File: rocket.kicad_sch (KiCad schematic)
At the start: 0 parts

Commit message: Place components
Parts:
- added A1: RaspberryPi_Pico, Module:RaspberryPi_Pico_Common_Unspecified, symbol MCU_Module:RaspberryPi_Pico
- added H1: MountingHole_Pad, MountingHole:MountingHole_2.2mm_M2_ISO7380_Pad_TopBottom, symbol Mechanical:MountingHole_Pad
- added H2, H3, H4: MountingHole_Pad, symbol Mechanical:MountingHole_Pad
- added J2: Micro_SD_Card, Connector_Card:microSD_HC_Wuerth_693072010801, symbol Connector:Micro_SD_Card
- added U1, U4: ICM-20948, Sensor_Motion:InvenSense_QFN-24_3x3mm_P0.4mm, symbol Sensor_Motion:ICM-20948
- added U2: RFM69HW, RF_Module:HOPERF_RFM69HW, symbol RF_Module:RFM69HW
- added U3: BMP390, 10LGA_2X2X0p75_BOS, symbol BMP390:BMP390
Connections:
- new net: U2.11 (GND), U2.9 (GND)
- new net: A1.13 (GND), A1.18 (GND), A1.23 (GND), A1.28 (GND), A1.3 (GND), A1.38 (GND), A1.8 (GND)
- new net: U4.18 (GND), U4.20 (GND)
- new net: U1.18 (GND), U1.20 (GND)
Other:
- title: (none) -> Rocketry Avionics Task

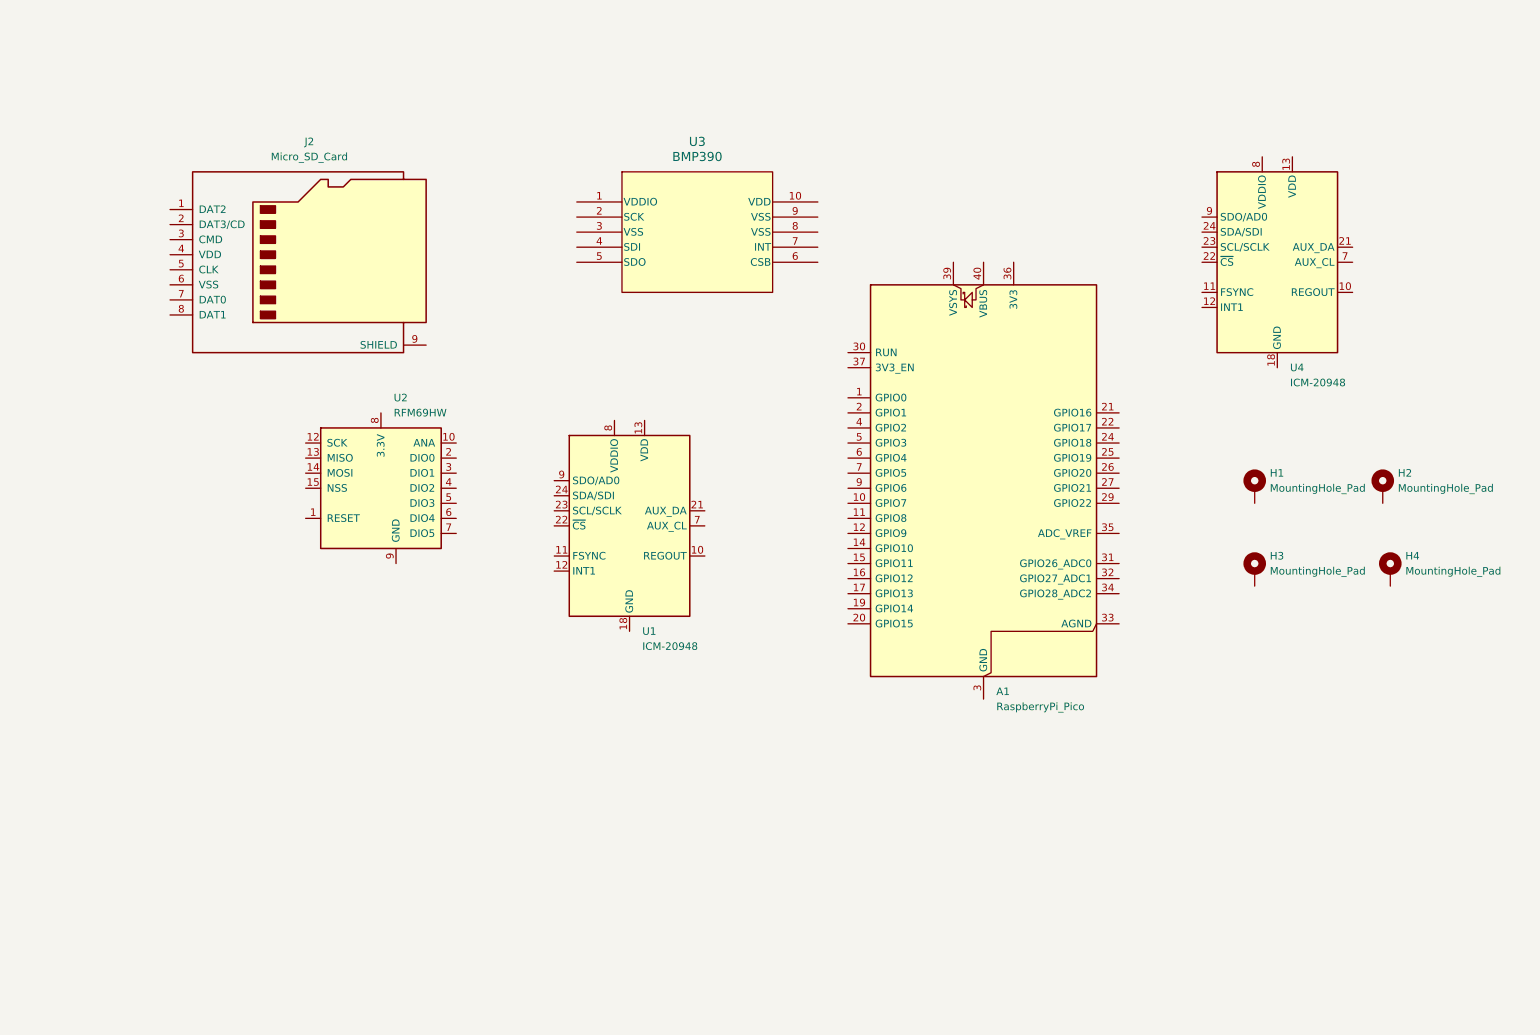
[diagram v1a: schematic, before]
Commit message: Logic level translators
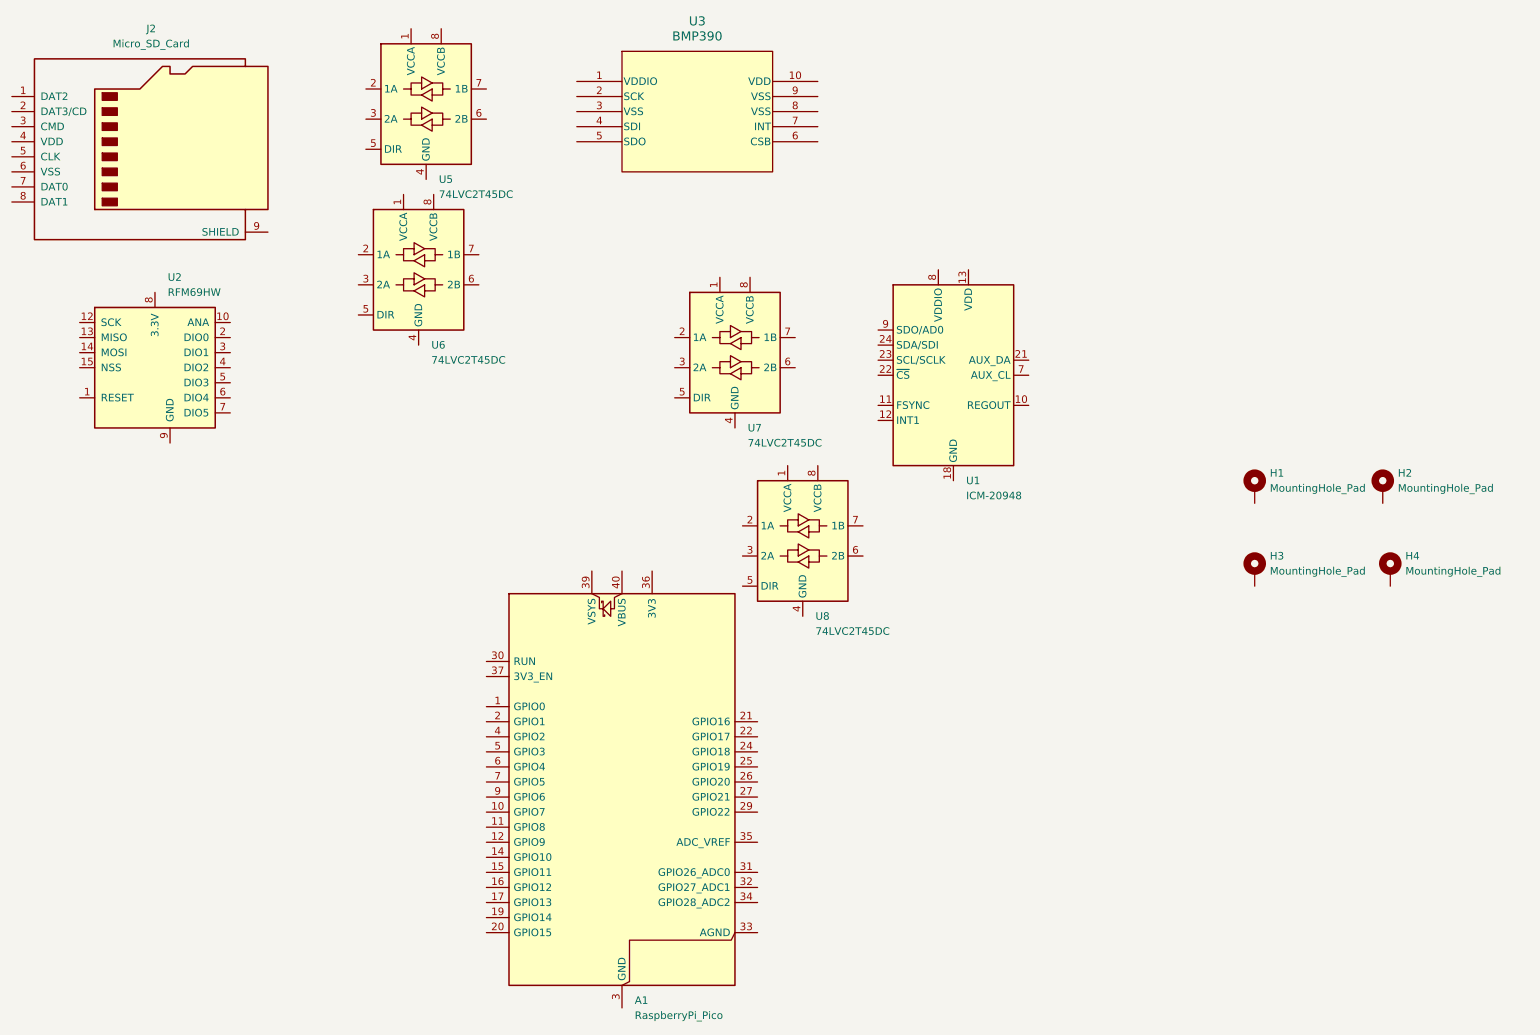
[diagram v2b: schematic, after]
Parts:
- removed U4: ICM-20948, Sensor_Motion:InvenSense_QFN-24_3x3mm_P0.4mm, symbol Sensor_Motion:ICM-20948
- added U5, U6, U7, U8: 74LVC2T45DC, Package_SO:VSSOP-8_2.3x2mm_P0.5mm, symbol Logic_LevelTranslator:74LVC2T45DC
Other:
- moved on the sheet: A1, J2, U1, U2, U3

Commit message: Wiring
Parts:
- removed J2: Micro_SD_Card, Connector_Card:microSD_HC_Wuerth_693072010801, symbol Connector:Micro_SD_Card
- removed U1: ICM-20948, Sensor_Motion:InvenSense_QFN-24_3x3mm_P0.4mm, symbol Sensor_Motion:ICM-20948
- removed U2: RFM69HW, RF_Module:HOPERF_RFM69HW, symbol RF_Module:RFM69HW
- removed U3: BMP390, 10LGA_2X2X0p75_BOS, symbol BMP390:BMP390
- removed U5, U6, U7, U8: 74LVC2T45DC, Package_SO:VSSOP-8_2.3x2mm_P0.5mm, symbol Logic_LevelTranslator:74LVC2T45DC
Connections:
- net Sensors/CS1: now reaches A1.12 (GPIO9)
- net Data Logging/VSS: now reaches A1.13 (GND), A1.18 (GND), A1.23 (GND), A1.28 (GND), A1.3 (GND), A1.38 (GND), A1.8 (GND)
- net Sensors/SCLK: now reaches A1.14 (GPIO10)
- net Sensors/MOSI: now reaches A1.15 (GPIO11)
- net Sensors/MISO: now reaches A1.16 (GPIO12)
- net Sensors/CS2: now reaches A1.17 (GPIO13)
- net Data Logging/CS1: now reaches A1.2 (GPIO1)
- net Data Logging/VDD: now reaches A1.36 (3V3)
- net Data Logging/SCLK: now reaches A1.4 (GPIO2)
- net Data Logging/MOSI: now reaches A1.5 (GPIO3)
- net Data Logging/MISO: now reaches A1.6 (GPIO4)
- net Data Logging/CS2: now reaches A1.7 (GPIO5)
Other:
- added sheet Data Logging (logging.kicad_sch)
- added sheet Sensors (sensors.kicad_sch)
- moved on the sheet: A1

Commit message: Power circuitry
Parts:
- removed H1: MountingHole_Pad, MountingHole:MountingHole_2.2mm_M2_ISO7380_Pad_TopBottom, symbol Mechanical:MountingHole_Pad
- removed H2: MountingHole_Pad, symbol Mechanical:MountingHole_Pad
- added H5, H6: MountingHole_Pad, MountingHole:MountingHole_2.5mm_Pad, symbol Mechanical:MountingHole_Pad
- added U1, U6: CPC1020N, Package_SO:SOP-4_3.8x4.1mm_P2.54mm, symbol Relay_SolidState:CPC1020N
- H3: renamed from H4; footprint (none) -> MountingHole:MountingHole_2.5mm_Pad
- H4: renamed from H3; footprint (none) -> MountingHole:MountingHole_2.5mm_Pad
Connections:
- net at H4.1: now also U1.4
- net at A1.21 (GPIO16): now also U1.1
- net at A1.22 (GPIO17): now also U6.1
- net Power circuitry/PGND: now reaches A1.33 (AGND)
- net Power circuitry/PGND: now also U1.2, U6.2
- net Power circuitry/7.4V: now reaches H3.1
- net Power circuitry/7.4V: now also H5.1
- new net: H6.1, U6.4
- new net Power circuitry/BGND: U1.3, U6.3
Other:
- added sheet Power circuitry (power.kicad_sch)
- moved on the sheet: H3, H4

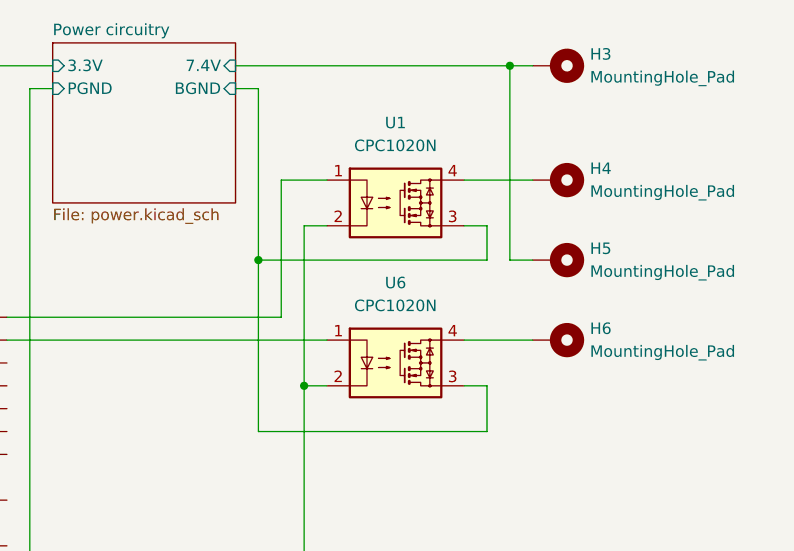
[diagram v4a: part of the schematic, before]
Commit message: Update references and switch to higher power MOSFETS
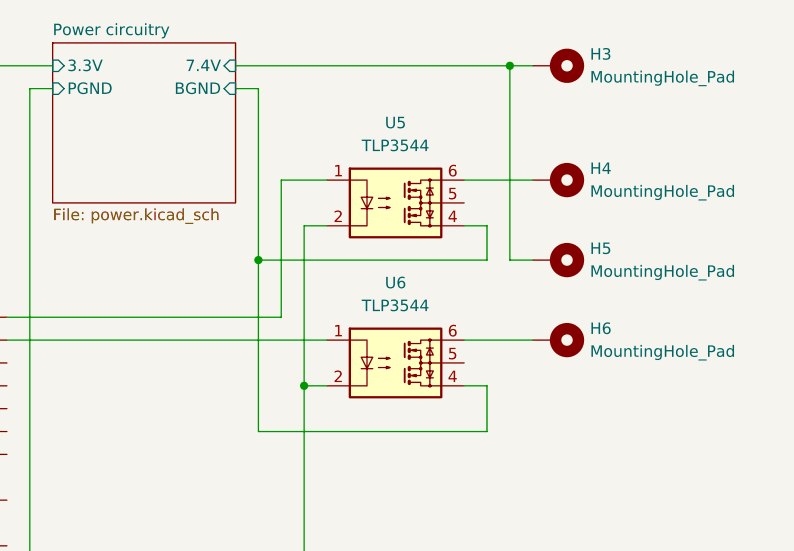
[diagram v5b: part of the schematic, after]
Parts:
- removed U1, U6: CPC1020N, Package_SO:SOP-4_3.8x4.1mm_P2.54mm, symbol Relay_SolidState:CPC1020N
- added U5, U6: TLP3544, Package_DIP:DIP-6_W7.62mm, symbol Relay_SolidState:TLP3544
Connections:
- net Power circuitry/BGND: now also U5.4, U6.4
- net Power circuitry/PGND: now also U5.2, U6.2
- net at H6.1: now also U6.6
- net at H4.1: now also U5.6
- net at A1.22 (GPIO17): now also U6.1
- net at A1.21 (GPIO16): now also U5.1
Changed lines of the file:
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@@
+	)
+	(symbol
+		(lib_id "Relay_SolidState:TLP3544")
+		(at 168.91 72.39 0)
+		(unit 1)
+		(exclude_from_sim no)
+		(in_bom yes)
+		(on_board yes)
+		(dnp no)
+		(fields_autoplaced yes)
+		(property "Reference" "U5"
+			(at 168.91 63.5 0)
+			(effects
+				(font
+					(size 1.27 1.27)
+				)
+			)
+		)
+		(property "Value" "TLP3544"
+			(at 168.91 66.04 0)
+			(effects
+				(font
+					(size 1.27 1.27)
+				)
+			)
+		)
+		(property "Footprint" "Package_DIP:DIP-6_W7.62mm"
+			(at 168.91 80.01 0)
+			(effects
+				(font
+					(size 1.27 1.27)
+				)
+				(hide yes)
+			)
+		)
+		(property "Datasheet" "https://toshiba.semicon-storage.com/info/docget.jsp?did=12661&prodName=TLP3544"
+			(at 168.91 72.39 0)
+			(effects
+				(font
+					(size 1.27 1.27)
+				)
+				(hide yes)
+			)
+		)
+		(property "Description" "Photo MOSFET optically coupled, ON 3.5A, 60mohm, OFF state 40V, Isolation 2500 VRMS, DIP-6"
+			(at 168.91 72.39 0)
+			(effects
+				(font
+					(size 1.27 1.27)
+				)
+				(hide yes)
+			)
+		)
+		(pin "4"
+		)
+		(pin "1"
+		)
+		(pin "5"
+		)
+		(pin "2"
+		)
+		(pin "6"
+		)
+		(pin "3"
+		)
+		(instances
+			(project ""
+				(path "/d94d1fd0-ec09-478b-a1a4-3306111fc872"
+					(reference "U5")
+					(unit 1)
+				)
+			)
+		)
 	)
 	(symbol
@@
 	)
 	(symbol
-		(lib_id "Relay_SolidState:CPC1020N")
+		(lib_id "Relay_SolidState:TLP3544")
 		(at 168.91 90.17 0)
 		(unit 1)
@@
 			)
 		)
-		(property "Value" "CPC1020N"
+		(property "Value" "TLP3544"
 			(at 168.91 83.82 0)
 			(effects
@@
 			)
 		)
-		(property "Footprint" "Package_SO:SOP-4_3.8x4.1mm_P2.54mm"
-			(at 168.91 95.504 0)
-			(effects
-				(font
-					(size 1.27 1.27)
-					(italic yes)
-				)
-				(hide yes)
-			)
-		)
-		(property "Datasheet" "https://www.littelfuse.com/assetdocs/littelfuse-integrated-circuits-cpc1020n-datasheet?assetguid=ccf92761-d571-4531-b987-0d7a91fc62dc"
-			(at 168.91 99.568 0)
-			(effects
-				(font
-					(size 1.27 1.27)
-				)
-				(hide yes)
-			)
-		)
-		(property "Description" "Form A, Solid State Relay (Photo MOSFET) 30V, 1.2A, 0.25Ohm, AC/DC, SO-4"
-			(at 168.91 97.536 0)
+		(property "Footprint" "Package_DIP:DIP-6_W7.62mm"
+			(at 168.91 97.79 0)
+			(effects
+				(font
+					(size 1.27 1.27)
+				)
+				(hide yes)
+			)
+		)
+		(property "Datasheet" "https://toshiba.semicon-storage.com/info/docget.jsp?did=12661&prodName=TLP3544"
+			(at 168.91 90.17 0)
+			(effects
+				(font
+					(size 1.27 1.27)
+				)
+				(hide yes)
+			)
+		)
+		(property "Description" "Photo MOSFET optically coupled, ON 3.5A, 60mohm, OFF state 40V, Isolation 2500 VRMS, DIP-6"
+			(at 168.91 90.17 0)
 			(effects
 				(font
@@
 		(pin "1"
 		)
+		(pin "5"
+		)
 		(pin "2"
+		)
+		(pin "6"
 		)
 		(pin "3"
@@
 					(unit 1)
 				)
-			)
-		)
-	)
-	(symbol
-		(lib_id "Relay_SolidState:CPC1020N")
-		(at 168.91 72.39 0)
-		(unit 1)
-		(exclude_from_sim no)
-		(in_bom yes)
-		(on_board yes)
-		(dnp no)
-		(fields_autoplaced yes)
-		(property "Reference" "U1"
-			(at 168.91 63.5 0)
-			(effects
-				(font
-					(size 1.27 1.27)
-				)
-			)
-		)
-		(property "Value" "CPC1020N"
-			(at 168.91 66.04 0)
-			(effects
-				(font
-					(size 1.27 1.27)
-				)
-			)
-		)
-		(property "Footprint" "Package_SO:SOP-4_3.8x4.1mm_P2.54mm"
-			(at 168.91 77.724 0)
-			(effects
-				(font
-					(size 1.27 1.27)
-					(italic yes)
-				)
-				(hide yes)
-			)
-		)
-		(property "Datasheet" "https://www.littelfuse.com/assetdocs/littelfuse-integrated-circuits-cpc1020n-datasheet?assetguid=ccf92761-d571-4531-b987-0d7a91fc62dc"
-			(at 168.91 81.788 0)
-			(effects
-				(font
-					(size 1.27 1.27)
-				)
-				(hide yes)
-			)
-		)
-		(property "Description" "Form A, Solid State Relay (Photo MOSFET) 30V, 1.2A, 0.25Ohm, AC/DC, SO-4"
-			(at 168.91 79.756 0)
-			(effects
-				(font
-					(size 1.27 1.27)
-				)
-				(hide yes)
-			)
-		)
-		(pin "4"
-		)
-		(pin "1"
-		)
-		(pin "2"
-		)
-		(pin "3"
-		)
-		(instances
-			(project ""
-				(path "/d94d1fd0-ec09-478b-a1a4-3306111fc872"
-					(reference "U1")
-					(unit 1)
-				)

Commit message: Begin PCB work
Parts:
- added R1, R2: 200Ω, Resistor_SMD:R_0201_0603Metric, symbol Device:R
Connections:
- net at U5.1: now also R1.2; no longer A1.21 (GPIO16)
- net at U6.1: now also R2.2; no longer A1.22 (GPIO17)
- new net: A1.21 (GPIO16), R1.1
- new net: A1.22 (GPIO17), R2.1
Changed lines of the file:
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@@
-	(wire
-		(pts
-			(xy 125.73 87.63) (xy 161.29 87.63)
-		)
-		(stroke
-			(width 0)
-			(type default)
-		)
-	)
 	(wire
 		(pts
@@
 	(wire
 		(pts
+			(xy 151.13 87.63) (xy 161.29 87.63)
+		)
+		(stroke
+			(width 0)
+			(type default)
+		)
+	)
+	(wire
+		(pts
 			(xy 38.1 83.82) (xy 38.1 77.47)
 		)
@@
 	(wire
 		(pts
+			(xy 140.97 85.09) (xy 156.21 85.09)
+		)
+		(stroke
+			(width 0)
+			(type default)
+		)
+	)
+	(wire
+		(pts
 			(xy 158.75 92.71) (xy 161.29 92.71)
 		)
@@
 	(wire
 		(pts
-			(xy 156.21 85.09) (xy 125.73 85.09)
-		)
-		(stroke
-			(width 0)
-			(type default)
-		)
-	)
-	(wire
-		(pts
 			(xy 64.77 113.03) (xy 80.01 113.03)
 		)
@@
 		(pts
 			(xy 64.77 92.71) (xy 80.01 92.71)
+		)
+		(stroke
+			(width 0)
+			(type default)
+		)
+	)
+	(wire
+		(pts
+			(xy 125.73 87.63) (xy 143.51 87.63)
+		)
+		(stroke
+			(width 0)
+			(type default)
+		)
+	)
+	(wire
+		(pts
+			(xy 125.73 85.09) (xy 133.35 85.09)
 		)
 		(stroke
@@
 	)
 	(symbol
+		(lib_id "Device:R")
+		(at 137.16 85.09 90)
+		(unit 1)
+		(exclude_from_sim no)
+		(in_bom yes)
+		(on_board yes)
+		(dnp no)
+		(property "Reference" "R1"
+			(at 137.16 80.01 90)
+			(effects
+				(font
+					(size 1.27 1.27)
+				)
+			)
+		)
+		(property "Value" "200Ω"
+			(at 137.16 82.55 90)
+			(effects
+				(font
+					(size 1.27 1.27)
+				)
+			)
+		)
+		(property "Footprint" "Resistor_SMD:R_0201_0603Metric"
+			(at 137.16 86.868 90)
+			(effects
+				(font
+					(size 1.27 1.27)
+				)
+				(hide yes)
+			)
+		)
+		(property "Datasheet" "~"
+			(at 137.16 85.09 0)
+			(effects
+				(font
+					(size 1.27 1.27)
+				)
+				(hide yes)
+			)
+		)
+		(property "Description" "Resistor"
+			(at 137.16 85.09 0)
+			(effects
+				(font
+					(size 1.27 1.27)
+				)
+				(hide yes)
+			)
+		)
+		(pin "2"
+		)
+		(pin "1"
+		)
+		(instances
+			(project ""
+				(path "/d94d1fd0-ec09-478b-a1a4-3306111fc872"
+					(reference "R1")
+					(unit 1)
+				)
+			)
+		)
+	)
+	(symbol
 		(lib_id "MCU_Module:RaspberryPi_Pico")
 		(at 102.87 97.79 0)
@@
 					(unit 1)
 				)
+			)
+		)
+	)
+	(symbol
+		(lib_id "Device:R")
+		(at 147.32 87.63 90)
+		(unit 1)
+		(exclude_from_sim no)
+		(in_bom yes)
+		(on_board yes)
+		(dnp no)
+		(property "Reference" "R2"
+			(at 147.32 80.01 90)
+			(effects
+				(font
+					(size 1.27 1.27)
+				)
+			)
+		)
+		(property "Value" "200Ω"
+			(at 147.32 82.55 90)
+			(effects
+				(font
+					(size 1.27 1.27)
+				)
+			)
+		)
+		(property "Footprint" "Resistor_SMD:R_0201_0603Metric"
+			(at 147.32 89.408 90)
+			(effects
+				(font
+					(size 1.27 1.27)
+				)
+				(hide yes)
+			)
+		)
+		(property "Datasheet" "~"
+			(at 147.32 87.63 0)
+			(effects
+				(font
+					(size 1.27 1.27)
+				)
+				(hide yes)
+			)
+		)
+		(property "Description" "Resistor"
+			(at 147.32 87.63 0)
+			(effects
+				(font
+					(size 1.27 1.27)
+				)
+				(hide yes)
+			)
+		)
+		(pin "2"
+		)
+		(pin "1"
+		)
+		(instances
+			(project "rocket"
+				(path "/d94d1fd0-ec09-478b-a1a4-3306111fc872"
+					(reference "R2")
+					(unit 1)
+				)
